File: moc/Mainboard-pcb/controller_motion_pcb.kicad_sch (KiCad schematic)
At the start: 30 parts, among them J1 Conn_01x09_Male, J2 Conn_01x09_Male, J3 Conn_01x06_Female, SW1 Rotary_Encoder_Switch, U1 TPIC6C595-SOIC, U2 TPIC6C595-SOIC

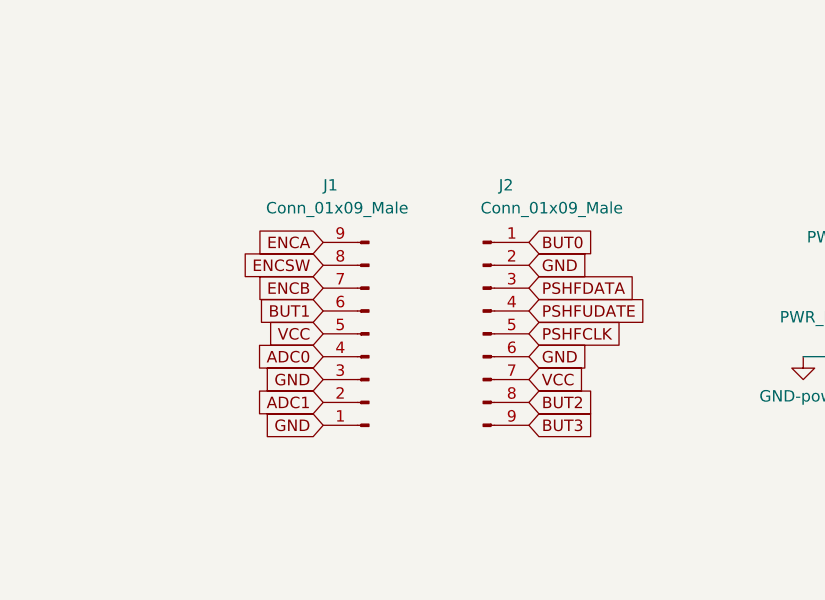
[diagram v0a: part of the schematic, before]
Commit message: split PCB Board
That's the final version for the split PCB board with 3 PCB Boards
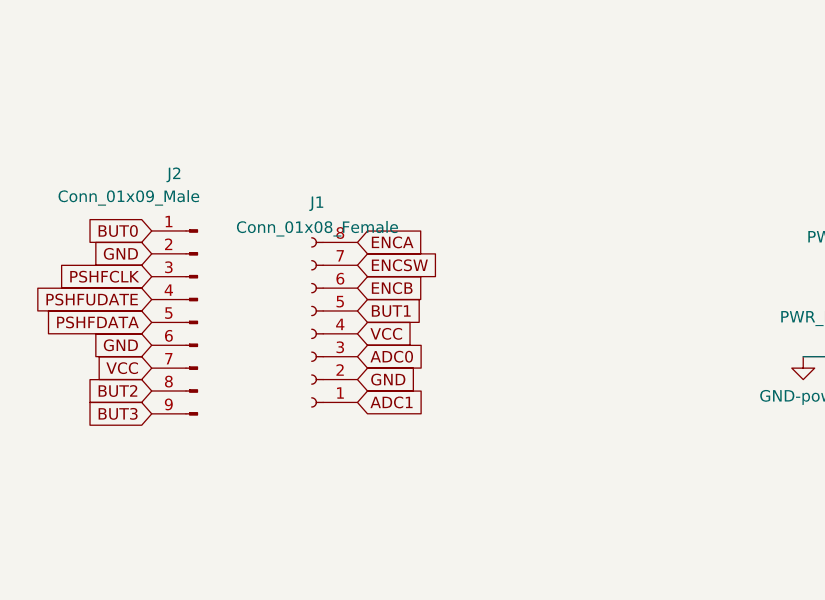
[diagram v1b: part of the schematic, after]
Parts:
- removed J1: Conn_01x09_Male, .Ambisonic:Header-01x09-p2.54-selfsolder, symbol Connector:Conn_01x09_Male
- added J1: Conn_01x08_Female, Connector_PinSocket_2.54mm:PinSocket_1x08_P2.54mm_Vertical, symbol Connector:Conn_01x08_Female
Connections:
- net ADC0: now also J1.3 (Pin_3)
- net ADC1: now also J1.1 (Pin_1)
- net BUT1: now also J1.5 (Pin_5)
- net ENCA: now also J1.8 (Pin_8)
- net ENCB: now also J1.6 (Pin_6)
- net ENCSW: now also J1.7 (Pin_7)
- net GND: now also J1.2 (Pin_2)
- net PSHFCLK: now also J2.3 (Pin_3); no longer J2.5 (Pin_5)
- net PSHFDATA: now also J2.5 (Pin_5); no longer J2.3 (Pin_3)
- net VCC: now also J1.4 (Pin_4)
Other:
- moved on the sheet: J2

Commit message: hardware io funzt
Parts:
- removed J1: Conn_01x08_Female, Connector_PinSocket_2.54mm:PinSocket_1x08_P2.54mm_Vertical, symbol Connector:Conn_01x08_Female
- removed J2: Conn_01x09_Male, .Ambisonic:Header-01x09-p2.54-selfsolder, symbol Connector:Conn_01x09_Male
- added C5: 10uF, Capacitor_THT:CP_Radial_D4.0mm_P1.50mm, symbol Device:CP
- added C6: 100nF, Capacitor_SMD:C_1206_3216Metric_Pad1.33x1.80mm_HandSolder, symbol Device:C
- added J1: SPI_Female, Connector_PinSocket_2.54mm:PinSocket_1x05_P2.54mm_Horizontal, symbol Connector:Conn_01x05_Female
- added J2: SPI_Male, Connector_PinHeader_2.54mm:PinHeader_1x05_P2.54mm_Horizontal, symbol Connector:Conn_01x05_Male
- added J4: UPDI_Interface, Connector_PinHeader_2.54mm:PinHeader_1x03_P2.54mm_Vertical, symbol Connector:Conn_01x03_Male
- added J5: Programm_Jumper, Connector_PinHeader_2.54mm:PinHeader_2x02_P2.54mm_Vertical, symbol Connector:Conn_01x04_Male
- added R1, R2, R?: 0R, symbol Device:R
- added R? (x4): 4k7, symbol Device:R
- added U3: ATtiny1626, .Ambisonic:attiny1626, symbol .Ambisonic:ATtiny1626
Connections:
- net ADC0: now also J3.3 (Pin_3), U3.4 (PA6/ADC6); no longer J3.4 (Pin_4)
- net ADC1: now also J3.1 (Pin_1), U3.6 (PB5/ADC8/CLKOUT); no longer J3.2 (Pin_2)
- net BUT1: now also R?.2
- net BUT2: now also R?.2
- net BUT3: now also S4.3 (COM_2), R?.2; no longer S4.4 (COM_2)
- net ENCA: now also U3.13 (PC1/ADC13/DO2)
- net ENCB: now also U3.8 (PB3)
- net ENCSW: now also R?.2
- net GND: now also J3.2 (Pin_2), J3.4 (Pin_4), S4.2 (COM_1), C5.2, C6.1, J1.5 (Pin_5), J2.5 (Pin_5), J4.1 (Pin_1), U3.20 (GND); no longer J3.1 (Pin_1), J3.3 (Pin_3), S4.1 (COM_1)
- net PSHFDATA: now also R1.2
- net PSHFUDATE: now also U3.9 (PB2)
- net S2_B: now also U1.12 (DARIN5); no longer U1.11 (DRAIN4)
- net S4_B: now also U2.12 (DARIN5); no longer U2.11 (DRAIN4)
- net VCC: now also J5.4 (Pin_4)
- net at U1.9 (SEROUT): now also R?.1; no longer U2.2 (SERIN)
- net PSHFCLK renamed PSFHCLK
- net PSFHCLK: now also R2.2
- new net: R?.1, U3.12 (PC0/ADC12/SCK2)
- new net: R1.1, U3.17 (PA1/ADC1/DO1)
- new net: R2.1, U3.19 (PA3/ADC3/SCK1)
- new net: R?.1, U3.2 (PA4/ADC4/SS1)
- new net: R?.1, U3.3 (PA5/ADC5)
- new net: R?.1, U3.7 (PB4/ADC9/RST)
- new net PSHFDATA2: R?.2, U2.2 (SERIN)
- new net SCL: J1.4 (Pin_4), J2.4 (Pin_4), U3.11 (PB0/ADC11/SCL)
- new net SDA: J1.3 (Pin_3), J2.3 (Pin_3), U3.10 (PB1/ADC10/SDA)
- new net UPDI: J5.2 (Pin_2), U3.16 (PA0/UPDI/RESET)
- new net UPDI_w: J1.2 (Pin_2), J2.2 (Pin_2), J4.2 (Pin_2), J5.1 (Pin_1)
- new net VCC_w: C5.1, C6.2, J1.1 (Pin_1), J2.1 (Pin_1), J4.3 (Pin_3), J5.3 (Pin_3), U3.1 (VCC)
- no-connect marks 13 -> 10
